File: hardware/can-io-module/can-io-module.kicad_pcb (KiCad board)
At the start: 2 copper layers, 96 x 86 mm, 1 part, among them J1 ECU_FCI_24P_RightAngle

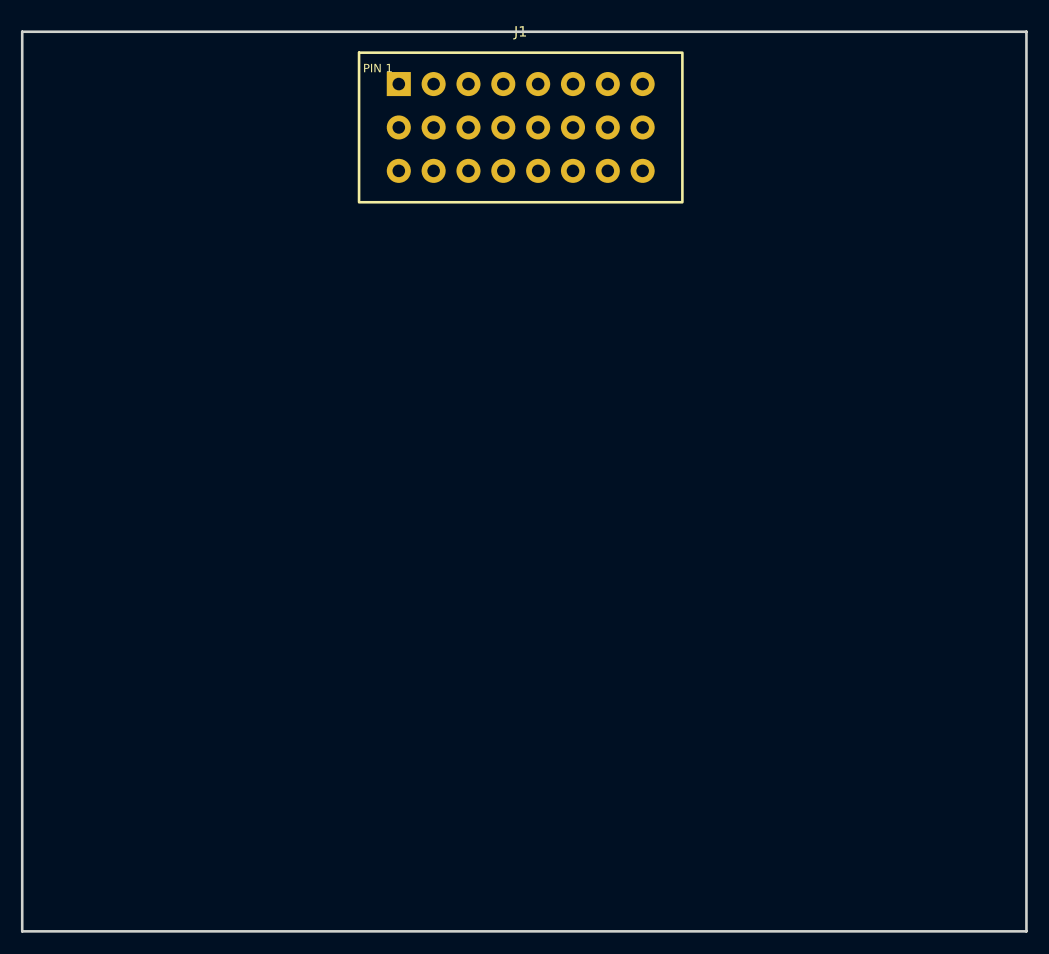
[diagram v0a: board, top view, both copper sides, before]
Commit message: feat: add CAN IO PCB placement and constraints
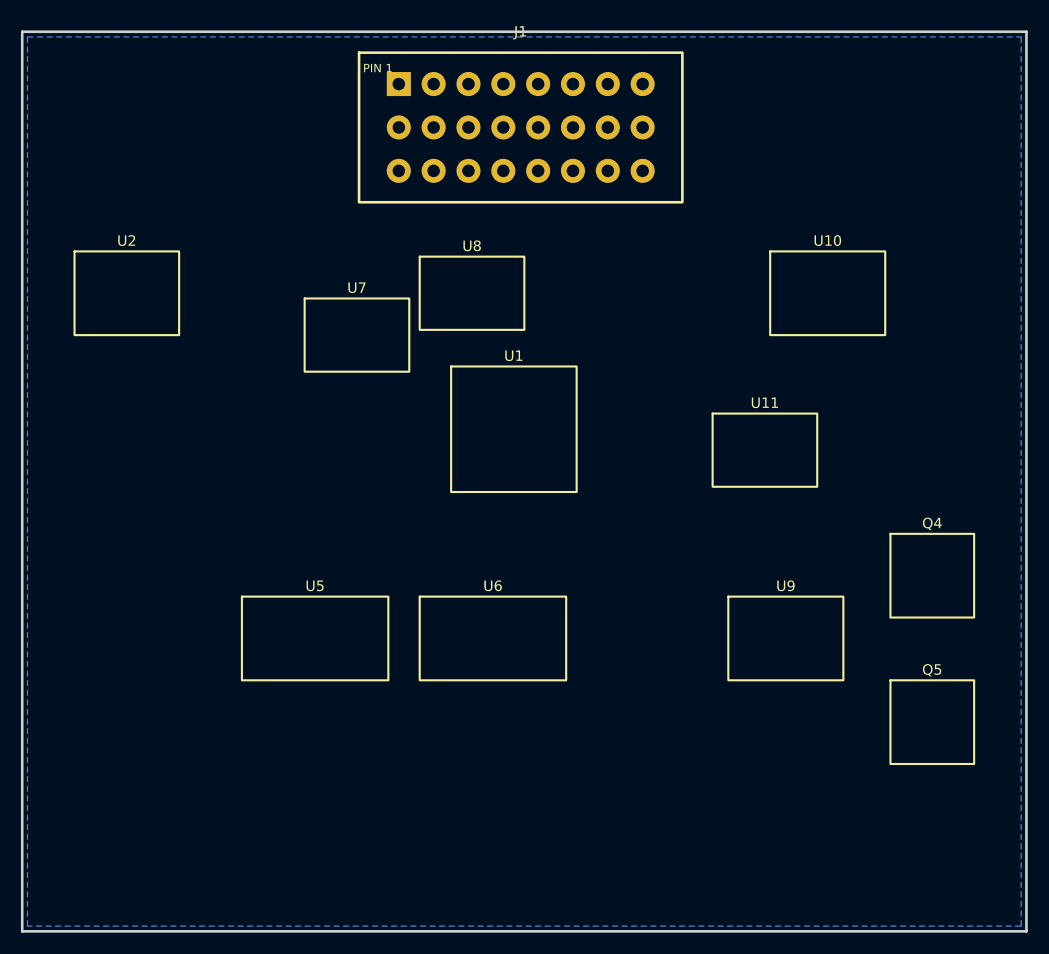
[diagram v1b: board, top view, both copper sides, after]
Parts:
- added Q4: RELAY1 MOSFET, DIY_DASH:PLACEMENT_BLOCK, F.Cu at (107.0, 72.0)
- added Q5: RELAY2 MOSFET, DIY_DASH:PLACEMENT_BLOCK, F.Cu at (107.0, 86.0)
- added U1: STM32G0B1CBT6, DIY_DASH:PLACEMENT_BLOCK, F.Cu at (67.0, 58.0)
- added U10: MAX31855K, DIY_DASH:PLACEMENT_BLOCK, F.Cu at (97.0, 45.0)
- added U11: FLEX SCHMITT, DIY_DASH:PLACEMENT_BLOCK, F.Cu at (91.0, 60.0)
- added U2: LMR16006Y-Q1, DIY_DASH:PLACEMENT_BLOCK, F.Cu at (30.0, 45.0)
- added U5: 74HCT4051-1K, DIY_DASH:PLACEMENT_BLOCK, F.Cu at (48.0, 78.0)
- added U6: 74HCT4051-4K7, DIY_DASH:PLACEMENT_BLOCK, F.Cu at (65.0, 78.0)
- added U7: L9613, DIY_DASH:PLACEMENT_BLOCK, F.Cu at (52.0, 49.0)
- added U8: TJA1051T/3, DIY_DASH:PLACEMENT_BLOCK, F.Cu at (63.0, 45.0)
- added U9: TLV9002-Q1, DIY_DASH:PLACEMENT_BLOCK, F.Cu at (93.0, 78.0)
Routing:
- added copper zone on B.Cu, net POWER_GND
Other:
- board text added: "BOTTOM POWER_GND PLANE"
- board text added: "BUCK SWITCH NODE KEEPOUT"
- board text added: "CAN TERM DEFAULT OPEN"
- board text added: "EGT COPPER KEEPOUT"
- board text added: "NETCLASS ANALOG WIDTH 0.20MM"
- board text added: "NETCLASS CAN DIFF 0.25MM GAP 0.20MM"
- board text added: "NETCLASS EGT WIDTH 0.20MM NO VIAS"
- board text added: "NETCLASS POWER WIDTH 0.60MM"
- board text added: "NETCLASS RELAY WIDTH 0.60MM"
- board text added: "PIN 1 VBAT"
- board text added: "PROTOTYPE REV A"
- board text added: "SWDIO SWCLK TP_NRST"
- board text added: "ZONE_ANALOG"
- board text added: "ZONE_EGT"
- board text added: "ZONE_MCU_COMMS"
- board text added: "ZONE_OUTPUTS"
- board text added: "ZONE_POWER"
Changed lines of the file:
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@@
     (pad "24" thru_hole oval (at 23.31 8.30) (size 2.3 2.3) (drill 1.2) (layers "*.Cu" "*.Mask") (net 24 "SERVICE") (pinfunction "SERVICE") (pintype "passive"))
+  )
+  (footprint "DIY_DASH:PLACEMENT_BLOCK" (layer "F.Cu")
+    (at 30 45)
+    (property "Reference" "U2" (at 0 -5.0) (layer "F.SilkS") (effects (font (size 1 1) (thickness 0.15))))
+    (property "Value" "LMR16006Y-Q1" (at 0 5.0) (layer "F.Fab") (effects (font (size 0.8 0.8) (thickness 0.12))))
+    (fp_rect (start -5.0 -4.0) (end 5.0 4.0) (stroke (width 0.2) (type default)) (fill none) (layer "F.SilkS"))
+  )
+  (footprint "DIY_DASH:PLACEMENT_BLOCK" (layer "F.Cu")
+    (at 67 58)
+    (property "Reference" "U1" (at 0 -7.0) (layer "F.SilkS") (effects (font (size 1 1) (thickness 0.15))))
+    (property "Value" "STM32G0B1CBT6" (at 0 7.0) (layer "F.Fab") (effects (font (size 0.8 0.8) (thickness 0.12))))
+    (fp_rect (start -6.0 -6.0) (end 6.0 6.0) (stroke (width 0.2) (type default)) (fill none) (layer "F.SilkS"))
+  )
+  (footprint "DIY_DASH:PLACEMENT_BLOCK" (layer "F.Cu")
+    (at 48 78)
+    (property "Reference" "U5" (at 0 -5.0) (layer "F.SilkS") (effects (font (size 1 1) (thickness 0.15))))
+    (property "Value" "74HCT4051-1K" (at 0 5.0) (layer "F.Fab") (effects (font (size 0.8 0.8) (thickness 0.12))))
+    (fp_rect (start -7.0 -4.0) (end 7.0 4.0) (stroke (width 0.2) (type default)) (fill none) (layer "F.SilkS"))
+  )
+  (footprint "DIY_DASH:PLACEMENT_BLOCK" (layer "F.Cu")
+    (at 65 78)
+    (property "Reference" "U6" (at 0 -5.0) (layer "F.SilkS") (effects (font (size 1 1) (thickness 0.15))))
+    (property "Value" "74HCT4051-4K7" (at 0 5.0) (layer "F.Fab") (effects (font (size 0.8 0.8) (thickness 0.12))))
+    (fp_rect (start -7.0 -4.0) (end 7.0 4.0) (stroke (width 0.2) (type default)) (fill none) (layer "F.SilkS"))
+  )
+  (footprint "DIY_DASH:PLACEMENT_BLOCK" (layer "F.Cu")
+    (at 52 49)
+    (property "Reference" "U7" (at 0 -4.5) (layer "F.SilkS") (effects (font (size 1 1) (thickness 0.15))))
+    (property "Value" "L9613" (at 0 4.5) (layer "F.Fab") (effects (font (size 0.8 0.8) (thickness 0.12))))
+    (fp_rect (start -5.0 -3.5) (end 5.0 3.5) (stroke (width 0.2) (type default)) (fill none) (layer "F.SilkS"))
+  )
+  (footprint "DIY_DASH:PLACEMENT_BLOCK" (layer "F.Cu")
+    (at 63 45)
+    (property "Reference" "U8" (at 0 -4.5) (layer "F.SilkS") (effects (font (size 1 1) (thickness 0.15))))
+    (property "Value" "TJA1051T/3" (at 0 4.5) (layer "F.Fab") (effects (font (size 0.8 0.8) (thickness 0.12))))
+    (fp_rect (start -5.0 -3.5) (end 5.0 3.5) (stroke (width 0.2) (type default)) (fill none) (layer "F.SilkS"))
+  )
+  (footprint "DIY_DASH:PLACEMENT_BLOCK" (layer "F.Cu")
+    (at 97 45)
+    (property "Reference" "U10" (at 0 -5.0) (layer "F.SilkS") (effects (font (size 1 1) (thickness 0.15))))
+    (property "Value" "MAX31855K" (at 0 5.0) (layer "F.Fab") (effects (font (size 0.8 0.8) (thickness 0.12))))
+    (fp_rect (start -5.5 -4.0) (end 5.5 4.0) (stroke (width 0.2) (type default)) (fill none) (layer "F.SilkS"))
+  )
+  (footprint "DIY_DASH:PLACEMENT_BLOCK" (layer "F.Cu")
+    (at 91 60)
+    (property "Reference" "U11" (at 0 -4.5) (layer "F.SilkS") (effects (font (size 1 1) (thickness 0.15))))
+    (property "Value" "FLEX SCHMITT" (at 0 4.5) (layer "F.Fab") (effects (font (size 0.8 0.8) (thickness 0.12))))
+    (fp_rect (start -5.0 -3.5) (end 5.0 3.5) (stroke (width 0.2) (type default)) (fill none) (layer "F.SilkS"))
+  )
+  (footprint "DIY_DASH:PLACEMENT_BLOCK" (layer "F.Cu")
+    (at 93 78)
+    (property "Reference" "U9" (at 0 -5.0) (layer "F.SilkS") (effects (font (size 1 1) (thickness 0.15))))
+    (property "Value" "TLV9002-Q1" (at 0 5.0) (layer "F.Fab") (effects (font (size 0.8 0.8) (thickness 0.12))))
+    (fp_rect (start -5.5 -4.0) (end 5.5 4.0) (stroke (width 0.2) (type default)) (fill none) (layer "F.SilkS"))
+  )
+  (footprint "DIY_DASH:PLACEMENT_BLOCK" (layer "F.Cu")
+    (at 107 72)
+    (property "Reference" "Q4" (at 0 -5.0) (layer "F.SilkS") (effects (font (size 1 1) (thickness 0.15))))
+    (property "Value" "RELAY1 MOSFET" (at 0 5.0) (layer "F.Fab") (effects (font (size 0.8 0.8) (thickness 0.12))))
+    (fp_rect (start -4.0 -4.0) (end 4.0 4.0) (stroke (width 0.2) (type default)) (fill none) (layer "F.SilkS"))
+  )
+  (footprint "DIY_DASH:PLACEMENT_BLOCK" (layer "F.Cu")
+    (at 107 86)
+    (property "Reference" "Q5" (at 0 -5.0) (layer "F.SilkS") (effects (font (size 1 1) (thickness 0.15))))
+    (property "Value" "RELAY2 MOSFET" (at 0 5.0) (layer "F.Fab") (effects (font (size 0.8 0.8) (thickness 0.12))))
+    (fp_rect (start -4.0 -4.0) (end 4.0 4.0) (stroke (width 0.2) (type default)) (fill none) (layer "F.SilkS"))
+  )
+  (gr_text "NETCLASS POWER WIDTH 0.60MM" (at 30 95) (layer "Cmts.User") (effects (font (size 0.8 0.8) (thickness 0.12))))
+  (gr_text "NETCLASS CAN DIFF 0.25MM GAP 0.20MM" (at 55 98) (layer "Cmts.User") (effects (font (size 0.8 0.8) (thickness 0.12))))
+  (gr_text "NETCLASS EGT WIDTH 0.20MM NO VIAS" (at 89 98) (layer "Cmts.User") (effects (font (size 0.8 0.8) (thickness 0.12))))
+  (gr_text "NETCLASS ANALOG WIDTH 0.20MM" (at 55 102) (layer "Cmts.User") (effects (font (size 0.8 0.8) (thickness 0.12))))
+  (gr_text "NETCLASS RELAY WIDTH 0.60MM" (at 92 102) (layer "Cmts.User") (effects (font (size 0.8 0.8) (thickness 0.12))))
+  (gr_text "BOTTOM POWER_GND PLANE" (at 68 105) (layer "Cmts.User") (effects (font (size 0.8 0.8) (thickness 0.12))))
+  (gr_text "EGT COPPER KEEPOUT" (at 100 53) (layer "Cmts.User") (effects (font (size 0.8 0.8) (thickness 0.12))))
+  (gr_text "BUCK SWITCH NODE KEEPOUT" (at 31 54) (layer "Cmts.User") (effects (font (size 0.8 0.8) (thickness 0.12))))
+  (gr_text "PROTOTYPE REV A" (at 28 25) (layer "Cmts.User") (effects (font (size 0.8 0.8) (thickness 0.12))))
+  (gr_text "PIN 1 VBAT" (at 48 23) (layer "Cmts.User") (effects (font (size 0.8 0.8) (thickness 0.12))))
+  (gr_text "CAN TERM DEFAULT OPEN" (at 92 28) (layer "Cmts.User") (effects (font (size 0.8 0.8) (thickness 0.12))))
+  (gr_text "SWDIO SWCLK TP_NRST" (at 70 67) (layer "Cmts.User") (effects (font (size 0.8 0.8) (thickness 0.12))))
+  (gr_text "ZONE_POWER" (at 30 60) (layer "Cmts.User") (effects (font (size 0.8 0.8) (thickness 0.12))))
+  (gr_text "ZONE_MCU_COMMS" (at 66 50) (layer "Cmts.User") (effects (font (size 0.8 0.8) (thickness 0.12))))
+  (gr_text "ZONE_ANALOG" (at 57 89) (layer "Cmts.User") (effects (font (size 0.8 0.8) (thickness 0.12))))
+  (gr_text "ZONE_EGT" (at 99 55) (layer "Cmts.User") (effects (font (size 0.8 0.8) (thickness 0.12))))
+  (gr_text "ZONE_OUTPUTS" (at 101 92) (layer "Cmts.User") (effects (font (size 0.8 0.8) (thickness 0.12))))
+  (zone (net 2) (net_name "POWER_GND") (layer "B.Cu")
+    (hatch edge 0.5) (connect_pads (clearance 0.25)) (min_thickness 0.25) (fill yes (thermal_gap 0.3) (thermal_bridge_width 0.3))
+    (polygon (pts (xy 20.5 20.5) (xy 115.5 20.5) (xy 115.5 105.5) (xy 20.5 105.5)))
+  )
+  (zone (net 0) (net_name "") (layers "F.Cu" "B.Cu")
+    (hatch edge 0.5) (keepout (tracks not_allowed) (vias not_allowed) (pads allowed) (copperpour not_allowed) (footprints allowed))
+    (polygon (pts (xy 91 38) (xy 110 38) (xy 110 55) (xy 91 55)))
   )
   (gr_rect (start 20 20) (end 116 106) (stroke (width 0.25) (type default)) (fill none) (layer "Edge.Cuts"))
